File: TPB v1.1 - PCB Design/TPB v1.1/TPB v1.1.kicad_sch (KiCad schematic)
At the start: 15 parts, among them CN1 TYPE-C-31-M-12, Q1 BC847, Q2 BC847, U2 CH340C

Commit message: Schematic v2
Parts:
- added C2, C3: 10uF, Capacitor_SMD:C_0603_1608Metric_Pad1.08x0.95mm_HandSolder, symbol Device:C
- added D1: Yellow, LED_SMD:LED_0805_2012Metric_Pad1.15x1.40mm_HandSolder, symbol Device:LED
- added D2: Green, LED_SMD:LED_0805_2012Metric_Pad1.15x1.40mm_HandSolder, symbol Device:LED
- added D3: LED, LED_SMD:LED_0805_2012Metric_Pad1.15x1.40mm_HandSolder, symbol Device:LED
- added J1: Conn_02x03_Top_Bottom, Connector_IDC:IDC-Header_2x03_P2.54mm_Vertical, symbol Connector_Generic:Conn_02x03_Top_Bottom
- added R10: 10K, LED_SMD:LED_0805_2012Metric_Pad1.15x1.40mm_HandSolder, symbol Device:R
- added R6, R7: 100R, Resistor_SMD:R_0603_1608Metric_Pad0.98x0.95mm_HandSolder, symbol Device:R
- added R8, R9: 10K, Resistor_SMD:R_0603_1608Metric_Pad0.98x0.95mm_HandSolder, symbol Device:R
- added SW1, SW2: SW_Push, Button_Switch_SMD:SW_SPST_TL3305C, symbol Switch:SW_Push
- gave numbers to parts that had none: 7
- renumbered R1 to R3, R3 to R5, U2 to U1
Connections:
- net +3V3: now also J1.1 (Pin_1), R10.2, R8.2, R9.2; no longer U1.16 (VCC), U1.4 (V3)
- net +5V: now also CN1.B4/A9 (VBUS), U1.16 (VCC), C3.1; no longer CN1.A9/B4 (VBUS)
- net EN: now also J1.6 (Pin_6), SW2.1
- net GND: now also C2.2, C3.2, D3.1 (K), J1.3 (Pin_3), SW1.2, SW2.2
- net IO0: now also J1.2 (Pin_2), SW1.1
- net at U1.2 (TXD): now also R6.1
- net at U1.3 (RXD): now also R7.1
- new net: D3.2 (A), R10.1
- new net: D1.2 (A), R8.1
- new net: D2.2 (A), R9.1
- new net: C2.1, U1.4 (V3)
- new net RX: D2.1 (K), J1.5 (Pin_5), R7.2
- new net TX: D1.1 (K), J1.4 (Pin_4), R6.2
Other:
- title: (none) -> TPB - TTL Programming Board
- moved on the sheet: C4, C5, C6, C7, U2

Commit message: PCB Layout v1
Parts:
- removed J1: Conn_02x03_Top_Bottom, Connector_IDC:IDC-Header_2x03_P2.54mm_Vertical, symbol Connector_Generic:Conn_02x03_Top_Bottom
- added J1: ~, Connector_IDC:IDC-Header_2x03_P2.54mm_Vertical, symbol Connector_Generic:Conn_02x03_Odd_Even
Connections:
- net +3V3: now also J1.1 (Pin_1)
- net EN: now also J1.6 (Pin_6)
- net GND: now also J1.5 (Pin_5)
- net IO0: now also J1.3 (Pin_3)
- net RX: now also J1.4 (Pin_4)
- net TX: now also J1.2 (Pin_2)
- net USB renamed USB_N
- net USB_N: no longer CN1.A6 (DP1), CN1.B6 (DP2), U1.5 (UD+)
- new net USB_P: CN1.A6 (DP1), CN1.B6 (DP2), U1.5 (UD+)
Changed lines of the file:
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@@
     (stroke (width 0) (type default))
   )
-  (label "USB" (at 85.09 45.72 0) (fields_autoplaced)
-    (effects (font (size 1.27 1.27)) (justify left bottom))
-    (property "USB" "USB_P" (at 85.09 46.99 0)
-      (effects (font (size 1.27 1.27) italic) (justify left))
-    )
+  (label "USB_P" (at 85.09 45.72 0) (fields_autoplaced)
+    (effects (font (size 1.27 1.27)) (justify left bottom))
   )
   (label "RX" (at 208.28 143.51 0) (fields_autoplaced)
@@
     (effects (font (size 1.27 1.27)) (justify left bottom))
   )
-  (label "USB" (at 85.09 53.34 0) (fields_autoplaced)
-    (effects (font (size 1.27 1.27)) (justify left bottom))
-    (property "USB" "USB_N" (at 85.09 54.61 0)
-      (effects (font (size 1.27 1.27) italic) (justify left))
-    )
+  (label "USB_N" (at 85.09 53.34 0) (fields_autoplaced)
+    (effects (font (size 1.27 1.27)) (justify left bottom))
   )
   (label "RX" (at 140.97 43.18 0) (fields_autoplaced)
@@
         (path "/df7e6eab-ed74-40af-aa84-c9efa9f1b01d"
           (reference "Q1") (unit 1)
+        )
+      )
+    )
+  )
+  (symbol (lib_id "Connector_Generic:Conn_02x03_Odd_Even") (at 196.85 143.51 0) (unit 1)
+    (in_bom yes) (on_board yes) (dnp no) (fields_autoplaced)
+    (property "Reference" "J1" (at 198.12 134.62 0)
+      (effects (font (size 1.27 1.27)))
+    )
+    (property "Value" "~" (at 198.12 137.16 0)
+      (effects (font (size 1.27 1.27)))
+    )
+    (property "Footprint" "Connector_IDC:IDC-Header_2x03_P2.54mm_Vertical" (at 196.85 143.51 0)
+      (effects (font (size 1.27 1.27)) hide)
+    )
+    (property "Datasheet" "~" (at 196.85 143.51 0)
+      (effects (font (size 1.27 1.27)) hide)
+    )
+    (pin "1")
+    (pin "2")
+    (pin "3")
+    (pin "4")
+    (pin "5")
+    (pin "6")
+    (instances
+      (project "TPB v1.1"
+        (path "/df7e6eab-ed74-40af-aa84-c9efa9f1b01d"
+          (reference "J1") (unit 1)
         )
       )
@@
         )
       )
-    )
-  )
-  (symbol (lib_id "Connector_Generic:Conn_02x03_Top_Bottom") (at 196.85 143.51 0) (unit 1)
-    (in_bom yes) (on_board yes) (dnp no) (fields_autoplaced)
-    (property "Reference" "J1" (at 198.12 134.62 0)
-      (effects (font (size 1.27 1.27)))
-    )
-    (property "Value" "Conn_02x03_Top_Bottom" (at 198.12 137.16 0)
-      (effects (font (size 1.27 1.27)))
-    )
-    (property "Footprint" "Connector_IDC:IDC-Header_2x03_P2.54mm_Vertical" (at 196.85 143.51 0)
-      (effects (font (size 1.27 1.27)) hide)
-    )
-    (property "Datasheet" "~" (at 196.85 143.51 0)
-      (effects (font (size 1.27 1.27)) hide)
-    )
-    (pin "1")
-    (pin "2")
-    (pin "3")
-    (pin "4")
-    (pin "5")
-    (pin "6")
-    (instances
-      (project "TPB v1.1"
-        (path "/df7e6eab-ed74-40af-aa84-c9efa9f1b01d"
-          (reference "J1") (unit 1)
-        )
-      )

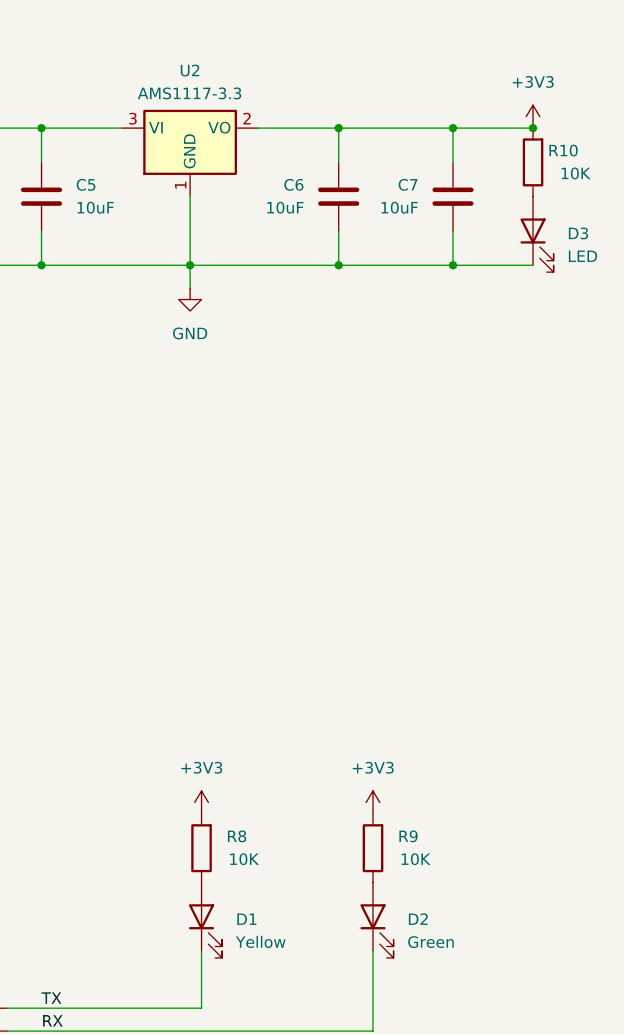
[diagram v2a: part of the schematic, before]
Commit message: Board Outline, Polygon and 3D of Buttons Added
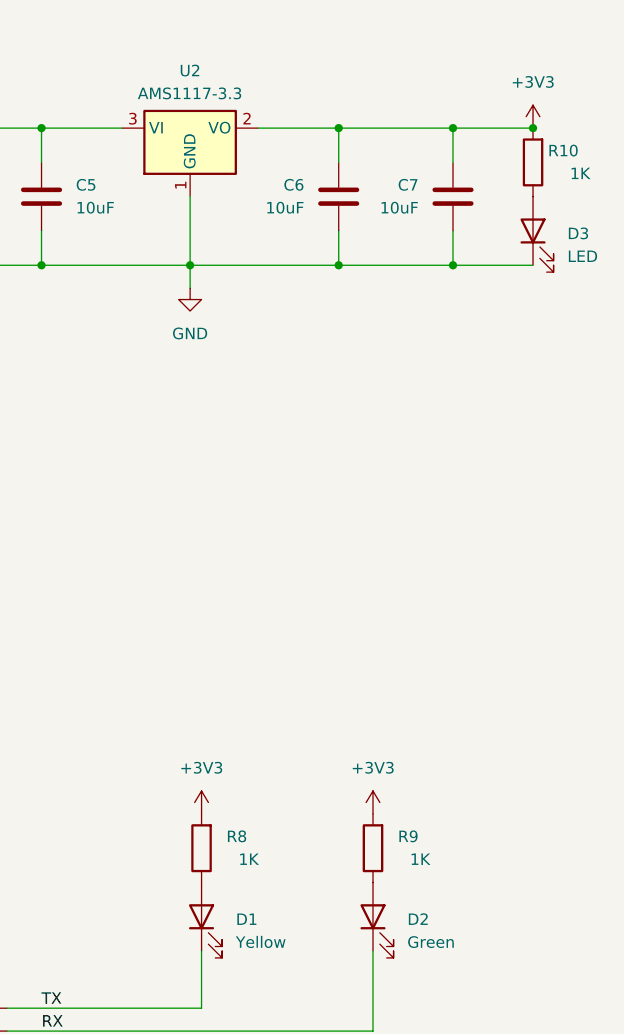
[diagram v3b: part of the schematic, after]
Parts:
- R10, R8, R9: value 10K -> 1K
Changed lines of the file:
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@@
       (effects (font (size 1.27 1.27)) (justify left))
     )
-    (property "Value" "10K" (at 232.41 124.46 0)
+    (property "Value" "1K" (at 232.41 124.46 0)
       (effects (font (size 1.27 1.27)) (justify left))
     )
@@
       (effects (font (size 1.27 1.27)) (justify left))
     )
-    (property "Value" "10K" (at 251.46 124.46 0)
+    (property "Value" "1K" (at 251.46 124.46 0)
       (effects (font (size 1.27 1.27)) (justify left))
     )
@@
       (effects (font (size 1.27 1.27)) (justify left))
     )
-    (property "Value" "10K" (at 269.24 48.26 0)
-      (effects (font (size 1.27 1.27)) (justify left))
-    )
+    (property "Value" "1K" (at 269.24 48.26 0)
+      (effects (font (size 1.27 1.27)) (justify left))
+    )
